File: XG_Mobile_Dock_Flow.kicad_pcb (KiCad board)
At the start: 4 copper layers, 220 x 65 mm, 97 parts, among them J1 5-1775443-8, J10 SWD, J11 UART, J12 I2C1, J13 39300240, J14 469911008, J17 8730, J2 20455-040E-76, J3 20455-040E-76, J4 3-2362375-4, J5 USB_C_Receptacle, Q16 AO3401A, Q17 2N7002W, SW1 SW_Push, U1 DS160PR410RNQR, U12 STM32F030C8Tx, U2 DS160PR410RNQR

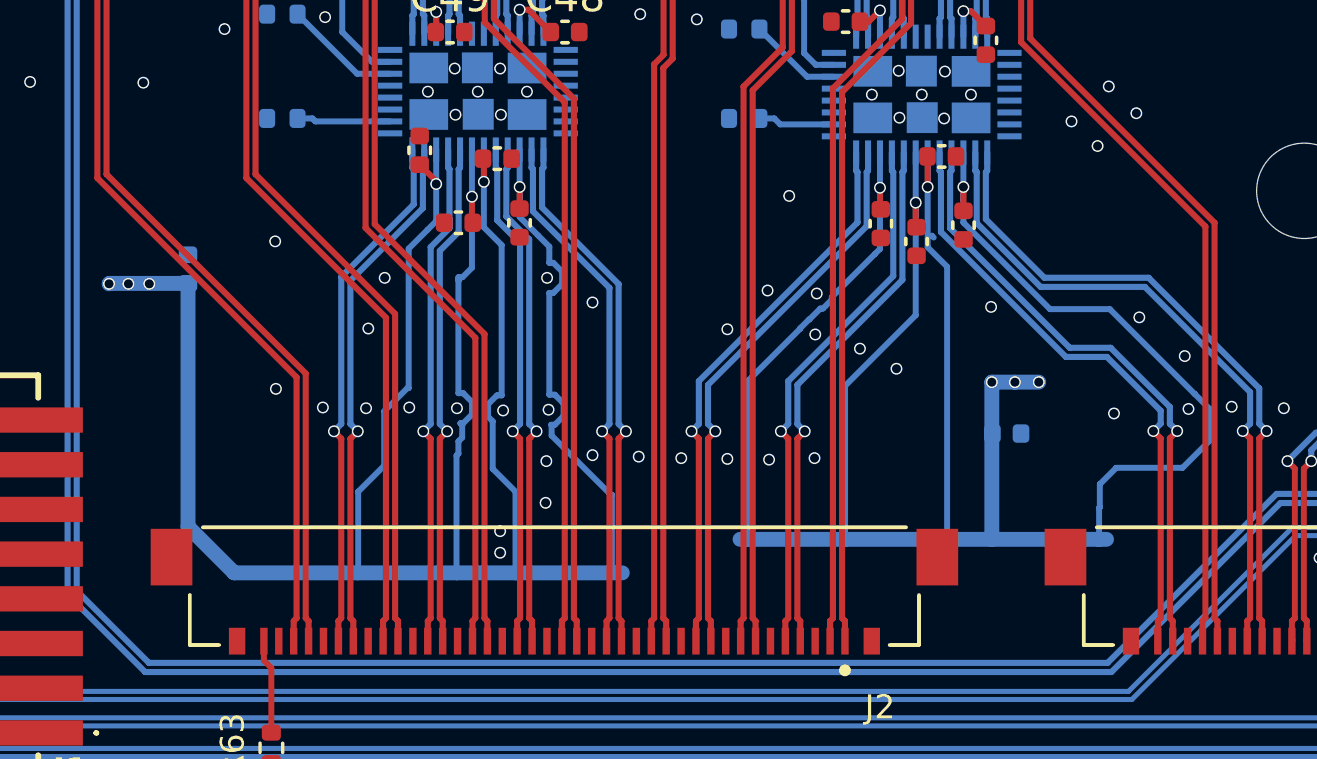
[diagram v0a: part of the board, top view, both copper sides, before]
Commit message: improved input voltage traces for redriver
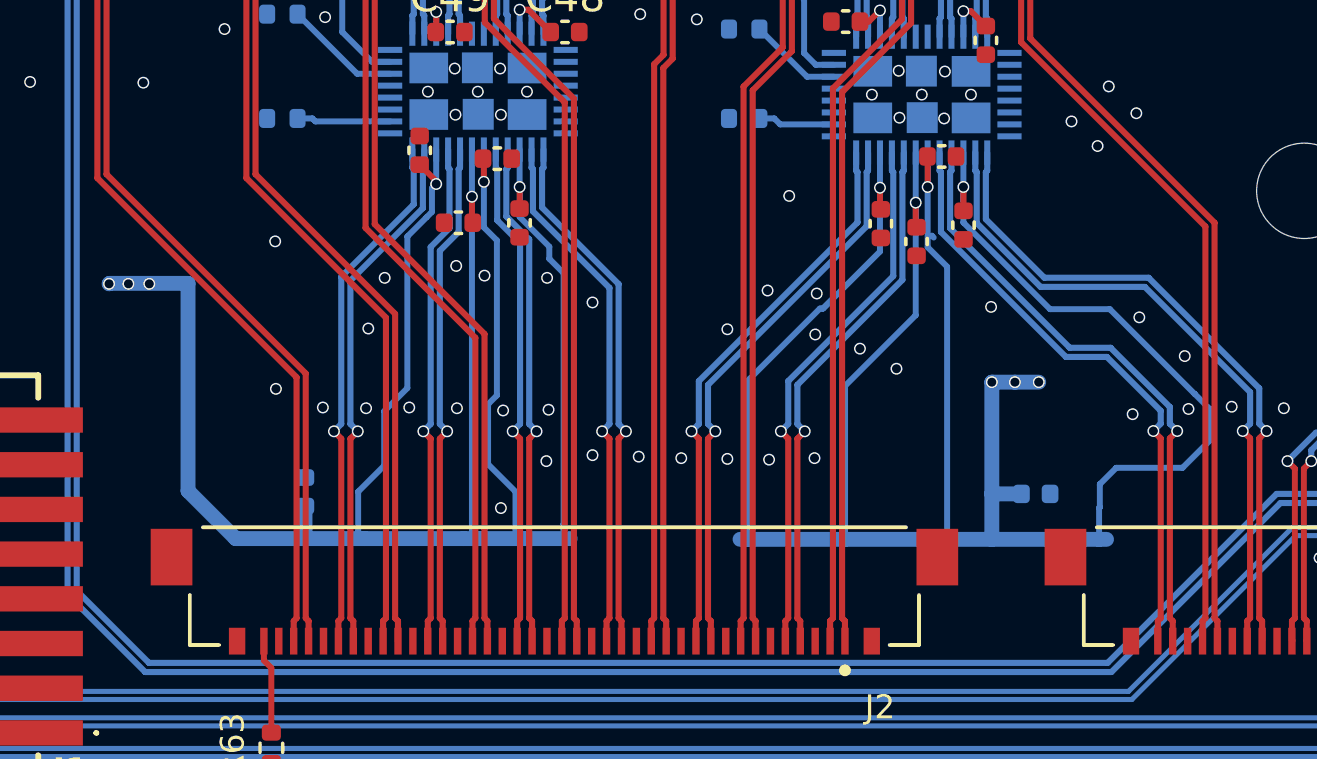
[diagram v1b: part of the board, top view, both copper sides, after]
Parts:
- moved C42 8.44 mm to (100.2, 82.0)
- moved C47 2.25 mm to (124.8, 82.1)
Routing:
- net +3V3: track 346.6 -> 338.9 mm

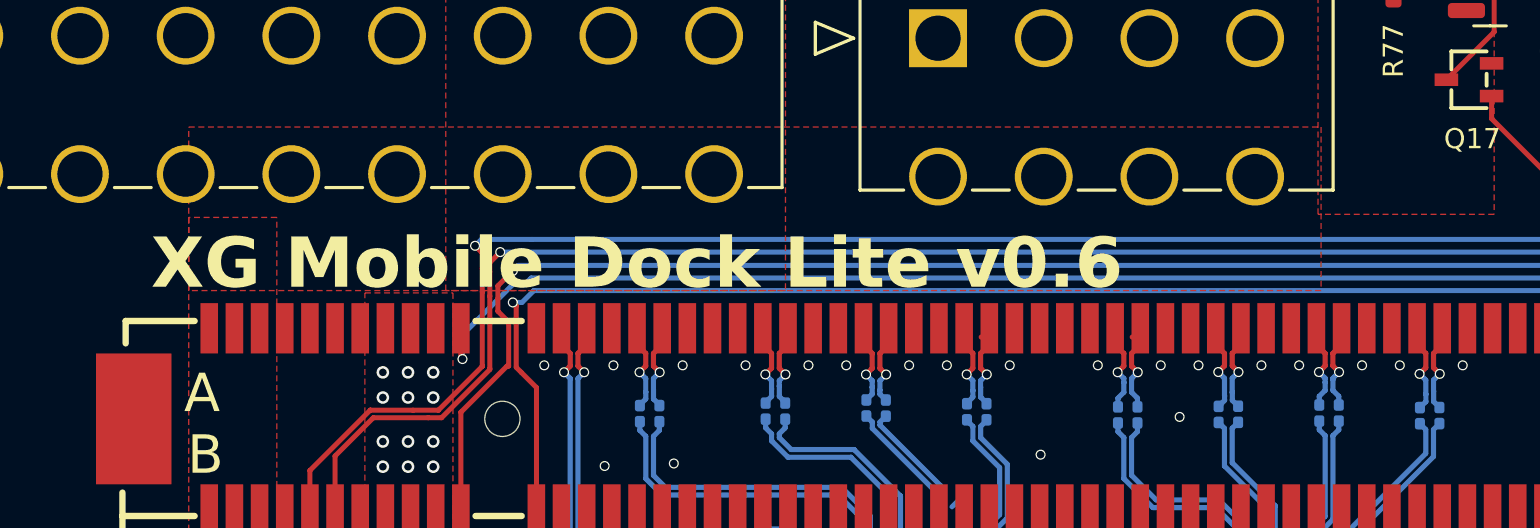
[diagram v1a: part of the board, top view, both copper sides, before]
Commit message: changed text on the pcb to match the name of the board
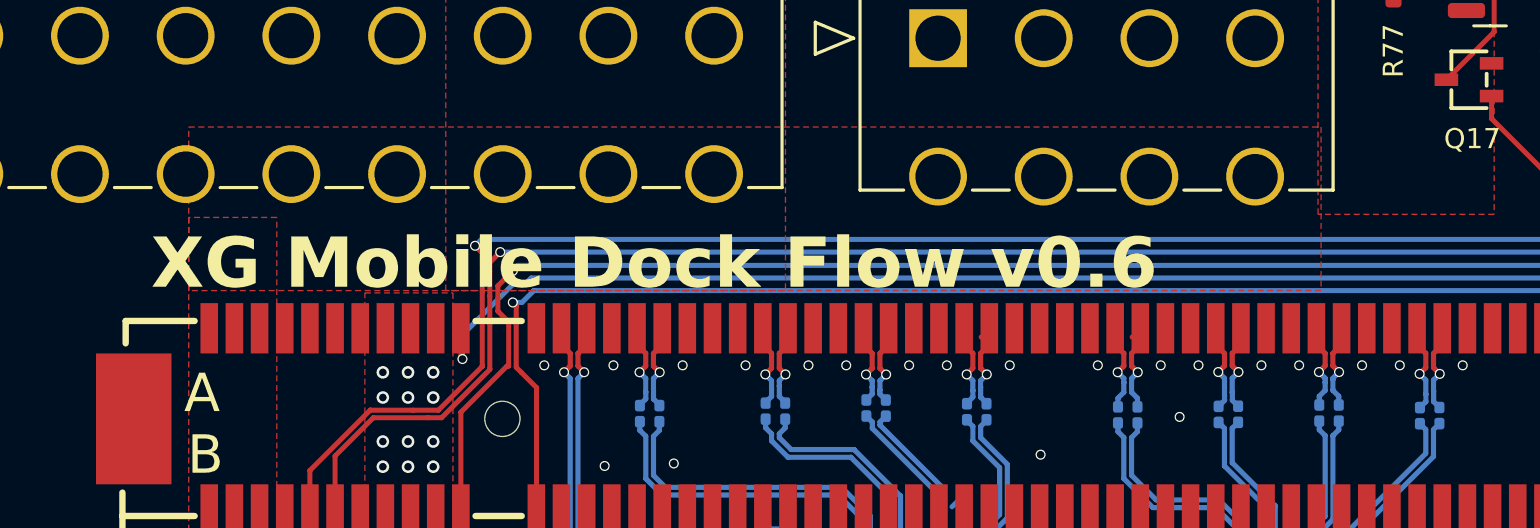
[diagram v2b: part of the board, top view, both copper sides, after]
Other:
- board text added: "XG Mobile Dock Flow v0.6"
- board text removed: "XG Mobile Dock Lite v0.6"
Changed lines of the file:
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@@
 		)
 	)
-	(gr_text "XG Mobile Dock Lite v0.6"
+	(gr_text "XG Mobile Dock Flow v0.6"
 		(at 75.621496 55.121496 0)
 		(layer "F.SilkS")

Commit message: added 3d models and more fine tunning
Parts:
- moved C40 1.03 mm to (120.6, 71.1), turned to 180 degrees
- moved C44 0.69 mm to (103.9, 71.2)
- moved C46 0.21 mm to (105.3, 72.8)
- moved C38 0.20 mm to (120.8, 73.4)
- moved C41 0.17 mm to (107.4, 72.8)
- moved C43 0.12 mm to (122.3, 73.0)
- moved C45 0.11 mm to (106.7, 71.0)
- moved C39 0.08 mm to (119.5, 73.0)
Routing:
- net +3V3: track 338.9 -> 374.8 mm
- net GND: track 6.51 -> 38.9 mm, vias 98 -> 103
- net /CLKP: track 87.0 -> 83.2 mm
- net /CLKN: track 84.8 -> 83.2 mm

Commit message: more fine tunning
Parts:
- moved R64 0.90 mm to (99.5, 66.9)
- moved R66 0.43 mm to (115.0, 66.9)
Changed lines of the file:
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@@
 	(footprint "Resistor_SMD:R_0402_1005Metric"
 		(layer "B.Cu")
-		(at 99.49 66 180)
+		(at 99.465 66.9 180)
 		(descr "Resistor SMD 0402 (1005 Metric), square (rectangular) end terminal, IPC_7351 nominal, (Body size source: IPC-SM-782 page 72, https://www.pcb-3d.com/wordpress/wp-content/uploads/ipc-sm-782a_amendment_1_and_2.pdf), generated with kicad-footprint-generator")
 		(tags "resistor")
@@
 	(footprint "Resistor_SMD:R_0402_1005Metric"
 		(layer "B.Cu")
-		(at 114.99 66.5 180)
+		(at 114.965 66.925 180)
 		(descr "Resistor SMD 0402 (1005 Metric), square (rectangular) end terminal, IPC_7351 nominal, (Body size source: IPC-SM-782 page 72, https://www.pcb-3d.com/wordpress/wp-content/uploads/ipc-sm-782a_amendment_1_and_2.pdf), generated with kicad-footprint-generator")
 		(tags "resistor")
@@
 	)
 	(via
-		(at 113.4 66.175)
+		(at 113.275 66)
 		(size 0.4)
 		(drill 0.3)
@@
 	)
 	(segment
-		(start 100 66)
-		(end 102 68)
+		(start 102 68)
+		(end 103.1072 68)
 		(width 0.2)
 		(layer "B.Cu")
@@
 	)
 	(segment
-		(start 102 68)
-		(end 103.1072 68)
+		(start 99.975 66.9)
+		(end 100.9 66.9)
+		(width 0.2)
+		(layer "B.Cu")
+		(net 190)
+	)
+	(segment
+		(start 100.9 66.9)
+		(end 102 68)
 		(width 0.2)
 		(layer "B.Cu")
@@
 	)
 	(segment
+		(start 115.475 66.925)
+		(end 115.925 66.925)
+		(width 0.2)
+		(layer "B.Cu")
+		(net 192)
+	)
+	(segment
 		(start 117.100001 68.100001)
 		(end 118 68.100001)
@@
 	)
 	(segment
-		(start 115.5 66.5)
+		(start 115.925 66.925)
 		(end 117.100001 68.100001)
 		(width 0.2)
